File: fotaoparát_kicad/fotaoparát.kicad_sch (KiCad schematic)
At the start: 35 parts, among them J1 Conn_01x08_Pin, J2 Conn_01x01_Socket, J3 Conn_01x01_Socket, J5 Conn_01x01_Socket, SW1 SW_MEC_5G, SW2 SW_MEC_5G, U1 TLV62569DBV, Y2 Crystal_GND24

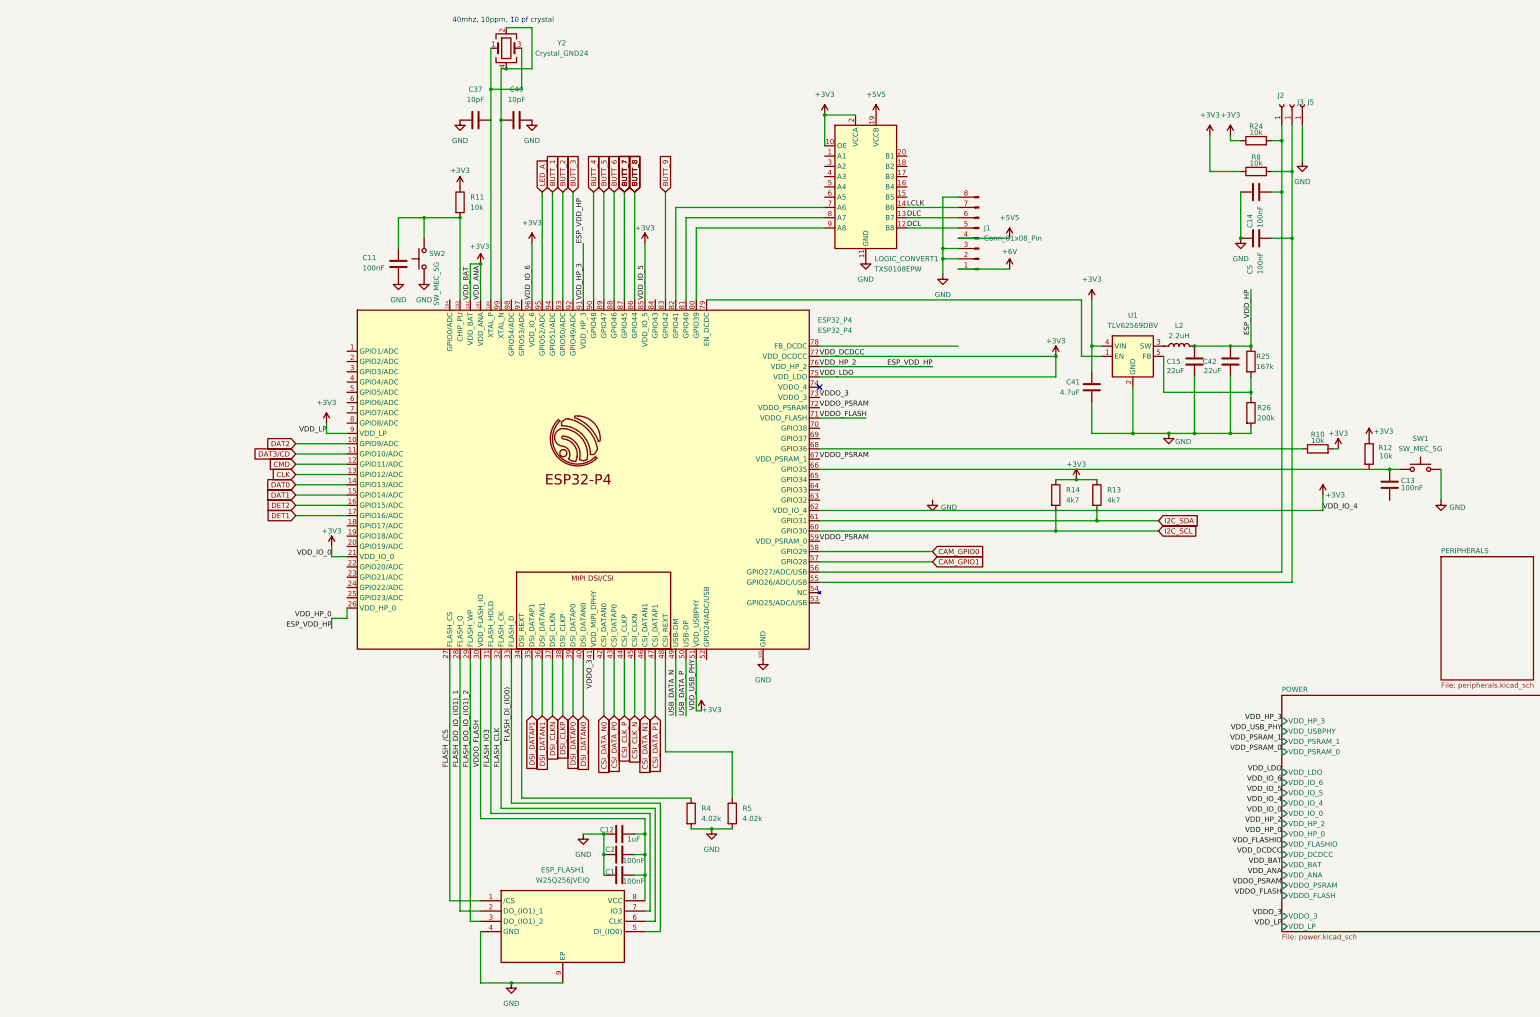
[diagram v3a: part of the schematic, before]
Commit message: [1/6] Úklid a opravy toho nejnutnějšího na hlavní straně schématu
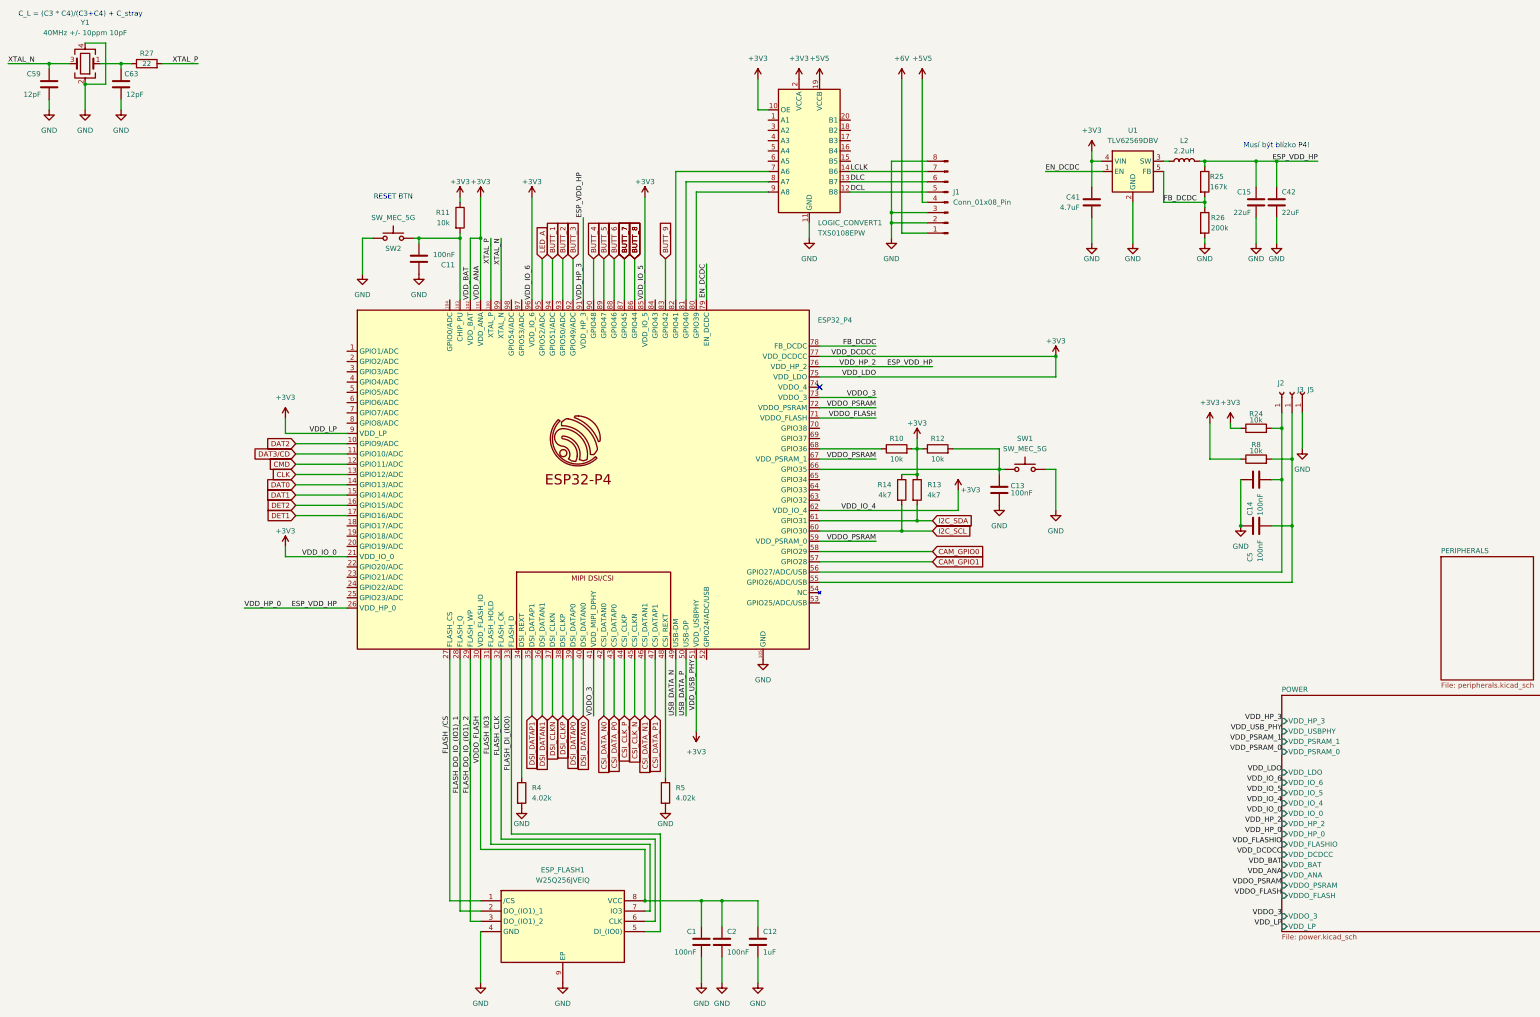
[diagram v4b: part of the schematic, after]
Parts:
- removed C37, C40: 10pF, Capacitor_SMD:C_0201_0603Metric, symbol Device:C
- removed Y2: Crystal_GND24, Crystal:Crystal_SMD_Abracon_ABM8G-4Pin_3.2x2.5mm, symbol Device:Crystal_GND24
- added C59, C63: 12pF, Capacitor_SMD:C_0402_1005Metric, symbol Device:C
- added R27: 22, Resistor_SMD:R_0402_1005Metric, symbol Device:R
- added Y1: 40MHz +/- 10ppm 10pF, Crystal:Crystal_SMD_2016-4Pin_2.0x1.6mm, symbol Device:Crystal_GND24
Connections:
- net GND: now also C11.1, C13.2, C59.2, C63.2, Y1.2, Y1.4; no longer C11.2
- net XTAL_P: now reaches ESP32_P4.100 (XTAL_P)
- net XTAL_P: now also R27.2
- net FB_DCDC: now reaches R25.2, R26.1, U1.5 (FB)
- net FB_DCDC: now also ESP32_P4.78 (FB_DCDC)
- net at ESP32_P4.103 (CHIP_PU), R11.2, SW2.3 (B)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: now also C11.2; no longer C11.1
- net EN_DCDC: now reaches ESP32_P4.79 (EN_DCDC), U1.1 (EN)
- net XTAL_N: now reaches ESP32_P4.99 (XTAL_N)
- net XTAL_N: now also C59.1, Y1.3
- new net: C63.1, R27.1, Y1.1
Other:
- note added: "C_L = (C3 * C4)/(C3+C4) + C_stray"
- note added: "Musí být blízko P4!"
- note added: "RESET BTN"
- note removed: "40mhz, 10ppm, 10 pf crystal"
- moved on the sheet: C1, C11, C12, C13, C14, C15, C2, C41, C42, C5, J1, J2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
